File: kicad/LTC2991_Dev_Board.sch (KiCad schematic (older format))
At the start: 12 parts, among them P1 CONN_01X08, P2 CONN_01X08, P3 CONN_02X03, P4 CONN_SENSE, Q1 MMBT3904, U1 LTC2991

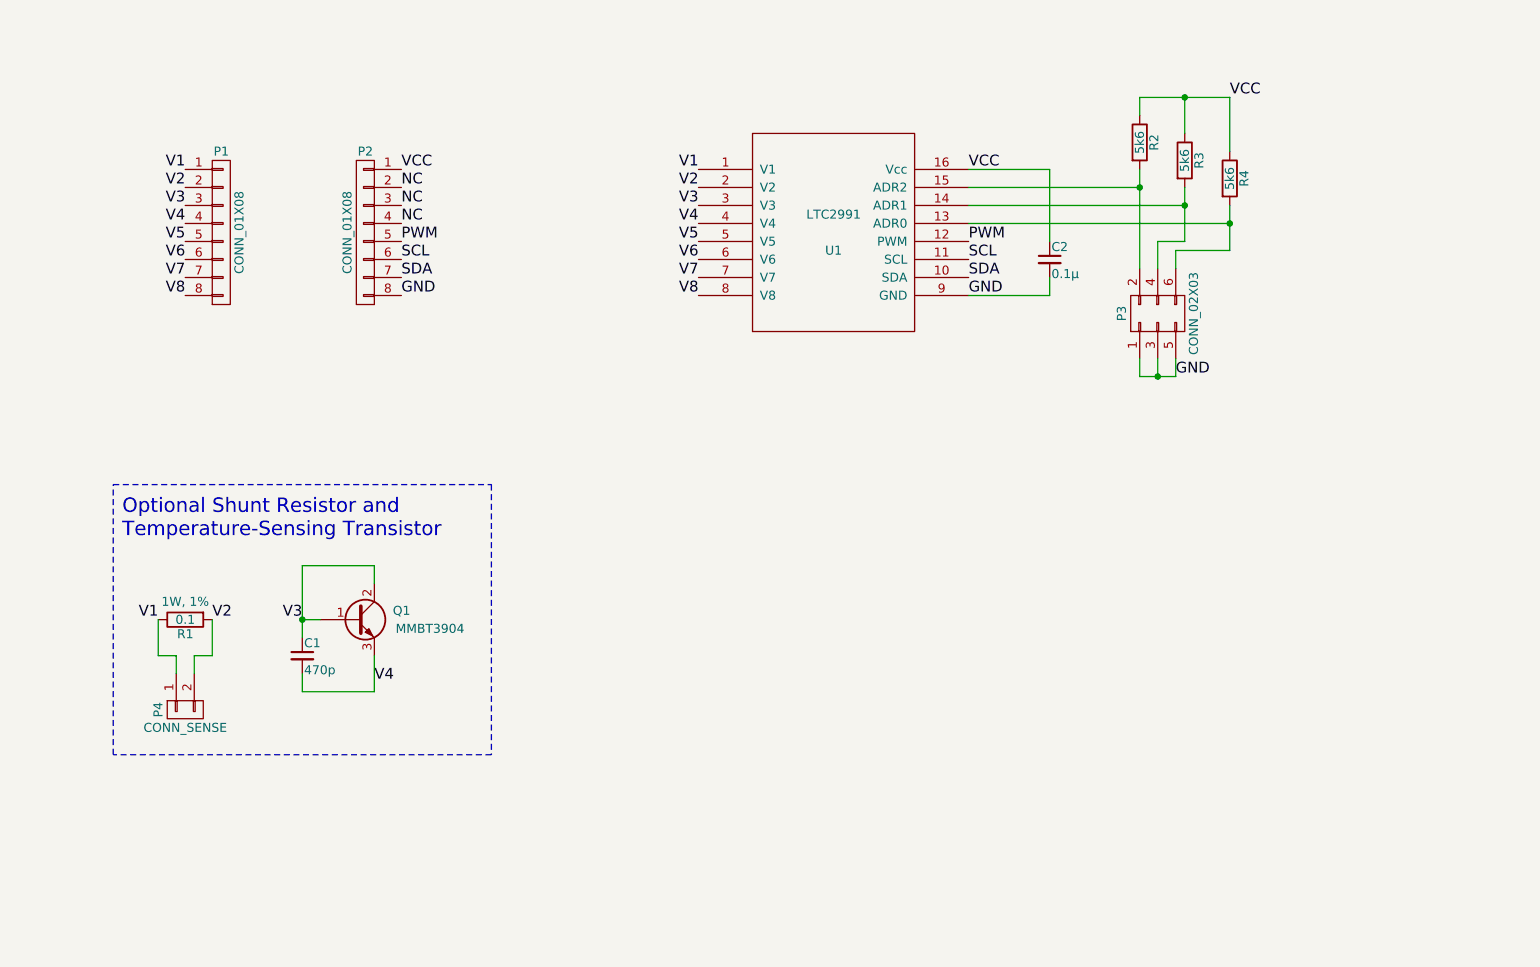
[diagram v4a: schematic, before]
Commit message: Rearranged schematic. In the hopes of making it a bit more readable. Updated PCB layout with new netlist (no significant changes).
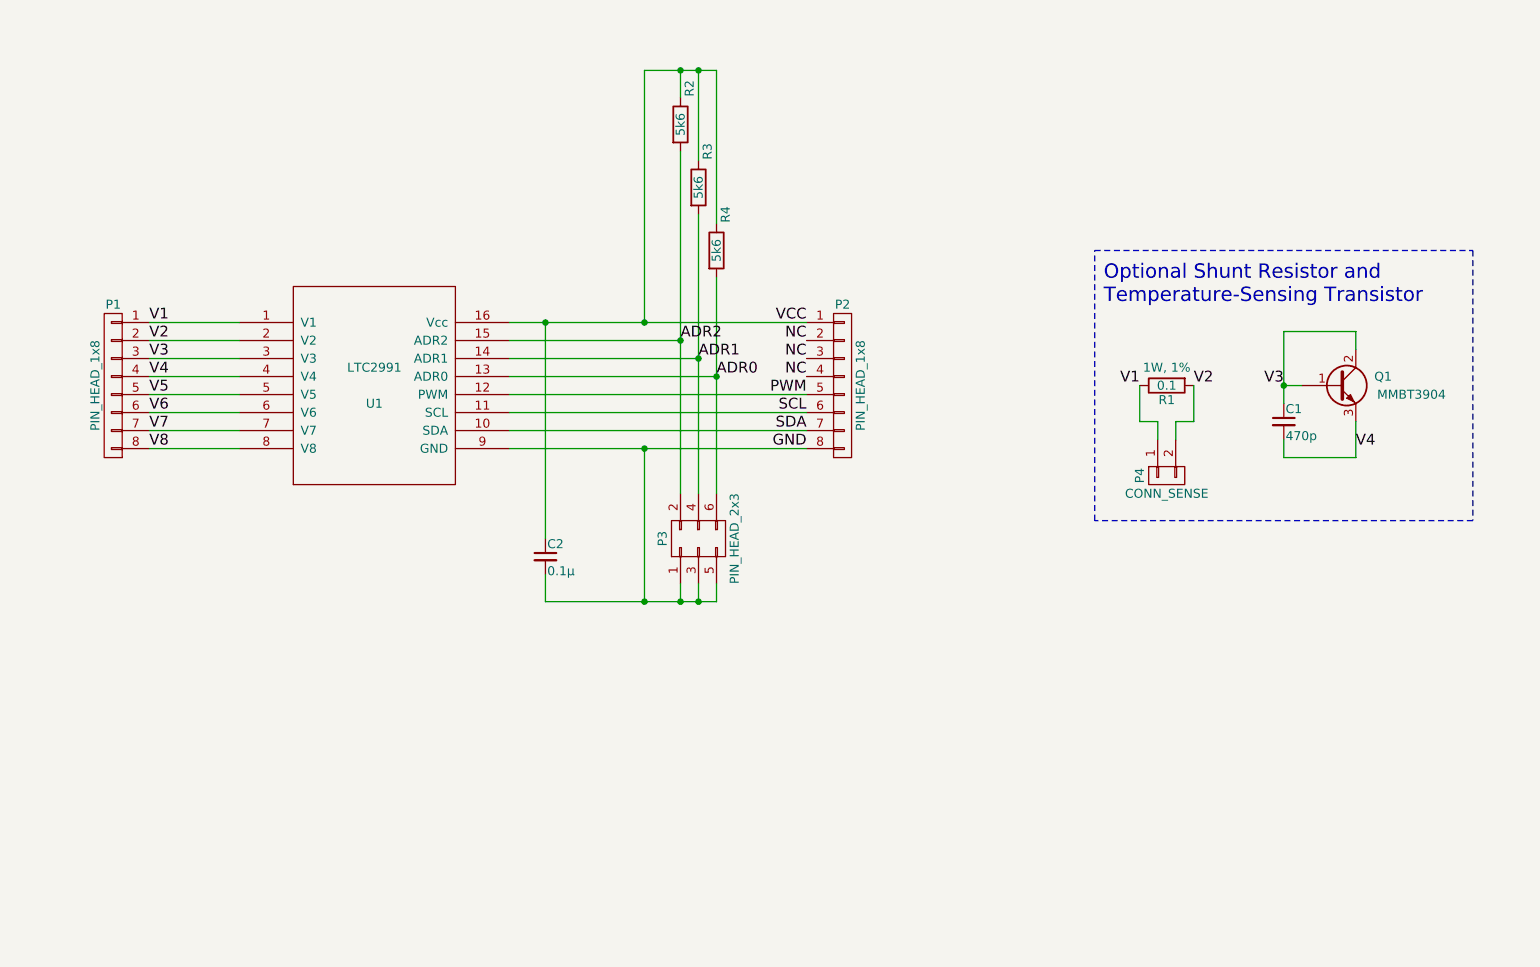
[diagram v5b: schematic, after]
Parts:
- P1, P2: value CONN_01X08 -> PIN_HEAD_1x8
- P3: value CONN_02X03 -> PIN_HEAD_2x3
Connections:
- net ADR0: now reaches P3.6 (P6), R4.2, U1.13 (ADR0)
- net ADR1: now reaches P3.4 (P4), R3.2, U1.14 (ADR1)
- net ADR2: now reaches P3.2 (P2), R2.2, U1.15 (ADR2)
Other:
- moved on the sheet: C1, C2, P1, P2, P3, P4, Q1, R1, R2, R3, R4, U1
